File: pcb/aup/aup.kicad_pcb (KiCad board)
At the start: 6 copper layers, 241.9 x 103 mm, 140 parts, among them IC1 MT41K128M16JT-125_K, IC2 88E1512-A0-NNP2C000, J1 DF40C-100DS-0.4V51, J1 DF40C-50DS-0.4V_51, J10 DF40C-50DS-0.4V_51, J11 DF40C-50DS-0.4V_51, J12 DF40C-50DS-0.4V_51, J2 DF40C-100DS-0.4V51, J2 DF40C-50DS-0.4V_51, J3 DF40C-100DS-0.4V51, J3 DF40C-50DS-0.4V_51, J4 DF40C-100DS-0.4V51, J4 DF40C-50DS-0.4V_51, J5 DF40C-40DS-0.4V51, J5 DF40C-50DS-0.4V_51, J6 DF40C-50DS-0.4V_51, J7 DF40C-50DS-0.4V_51, J8 DF40C-50DS-0.4V_51, J9 DF40C-50DS-0.4V_51, Q1 AO3401A, Q2 AO3400A, Q3 AO3401A, U1 XC7A50T-FGG484, U10 TPS2116DRLR, U11 FT2232HQ, U12 93LC56BT-I/OT, U13 MX25L3233FM2, U14 ISL80103IRAJZ-TK, U15 TPS2116DRLR, U2 USBLC6-2SC6, U3 TPS563257DRLR, U5 TPS563257DRLR, U6 ISL80103IRAJZ-TK, U7 TPS563257DRLR, U8 TPS563257DRLR, U9 TPS563257DRLR, Y1 12MHz/20pf

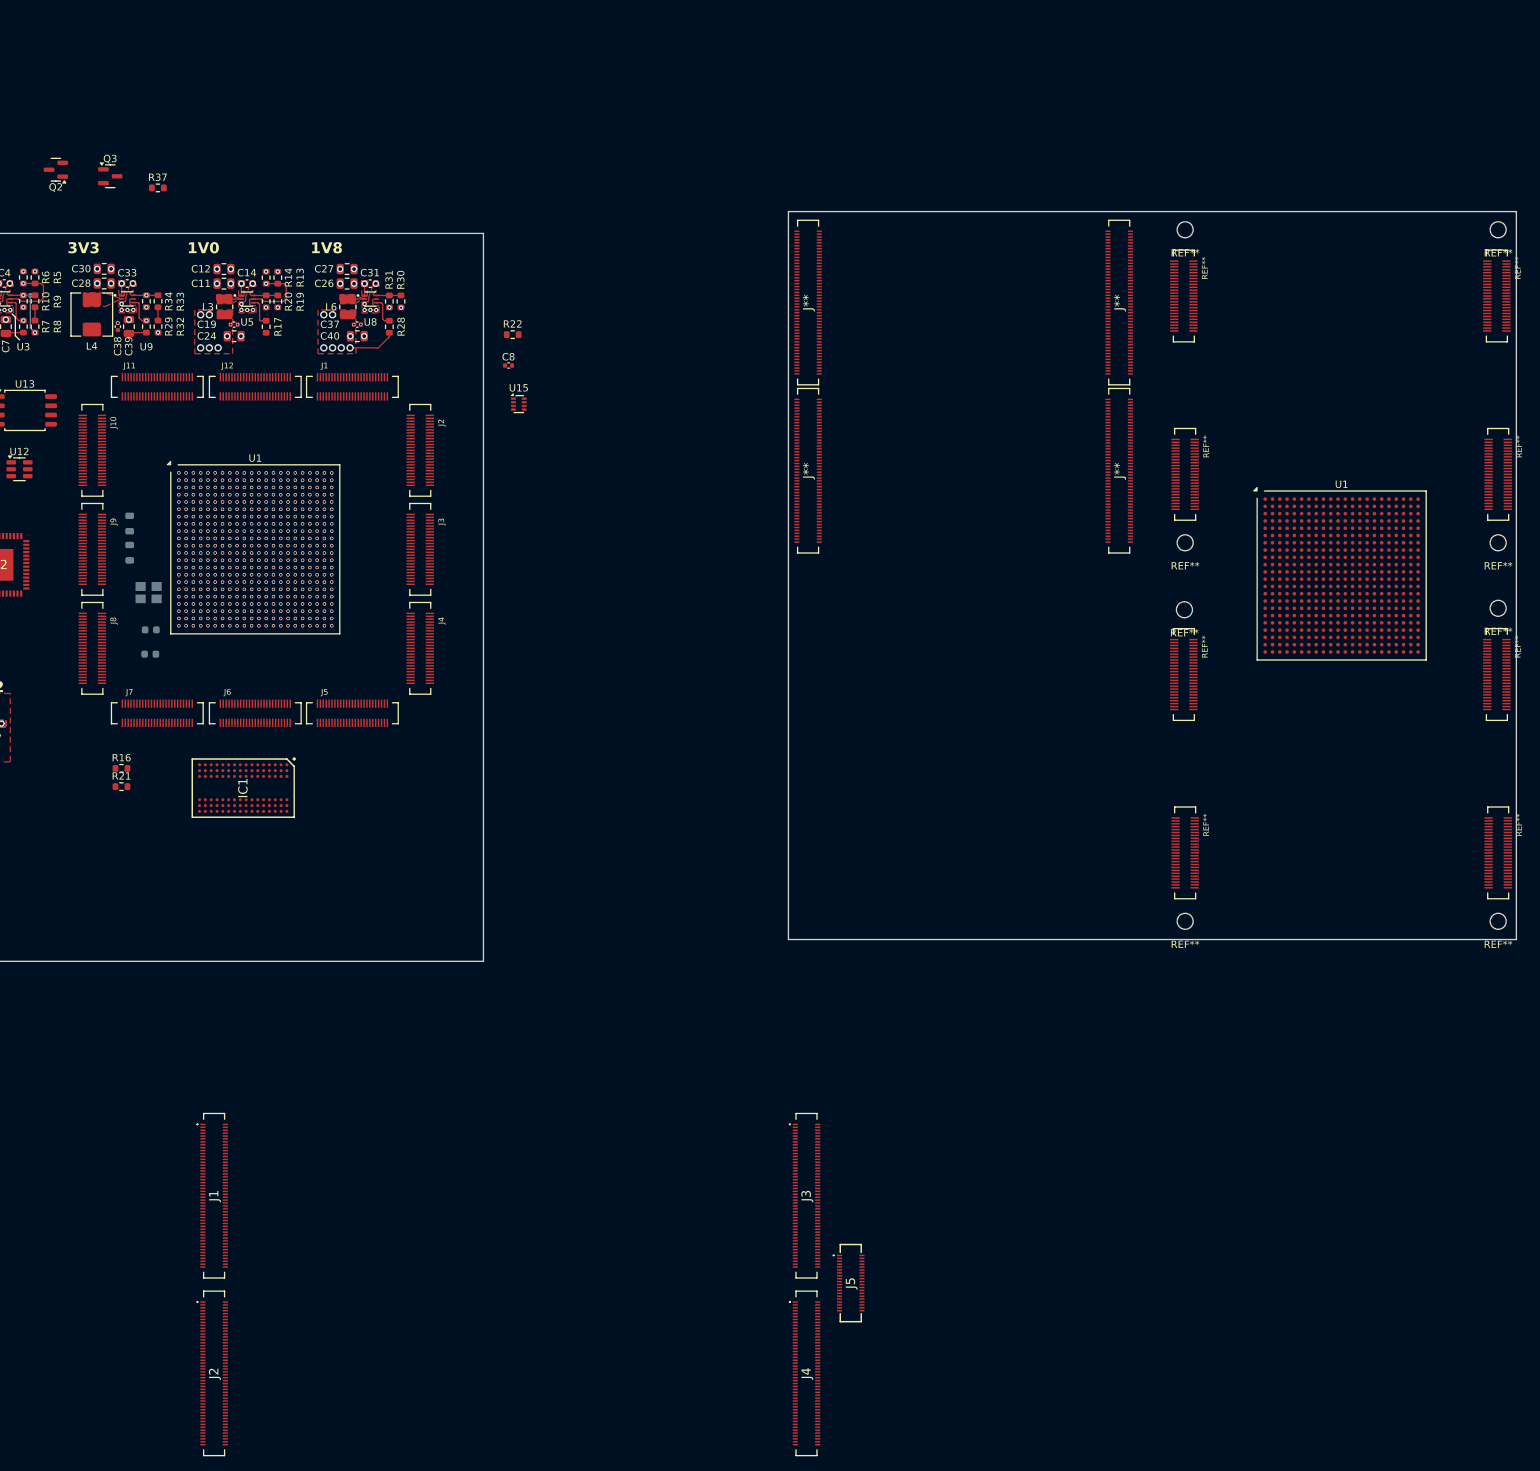
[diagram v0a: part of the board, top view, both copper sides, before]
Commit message: Switch to QSH-60
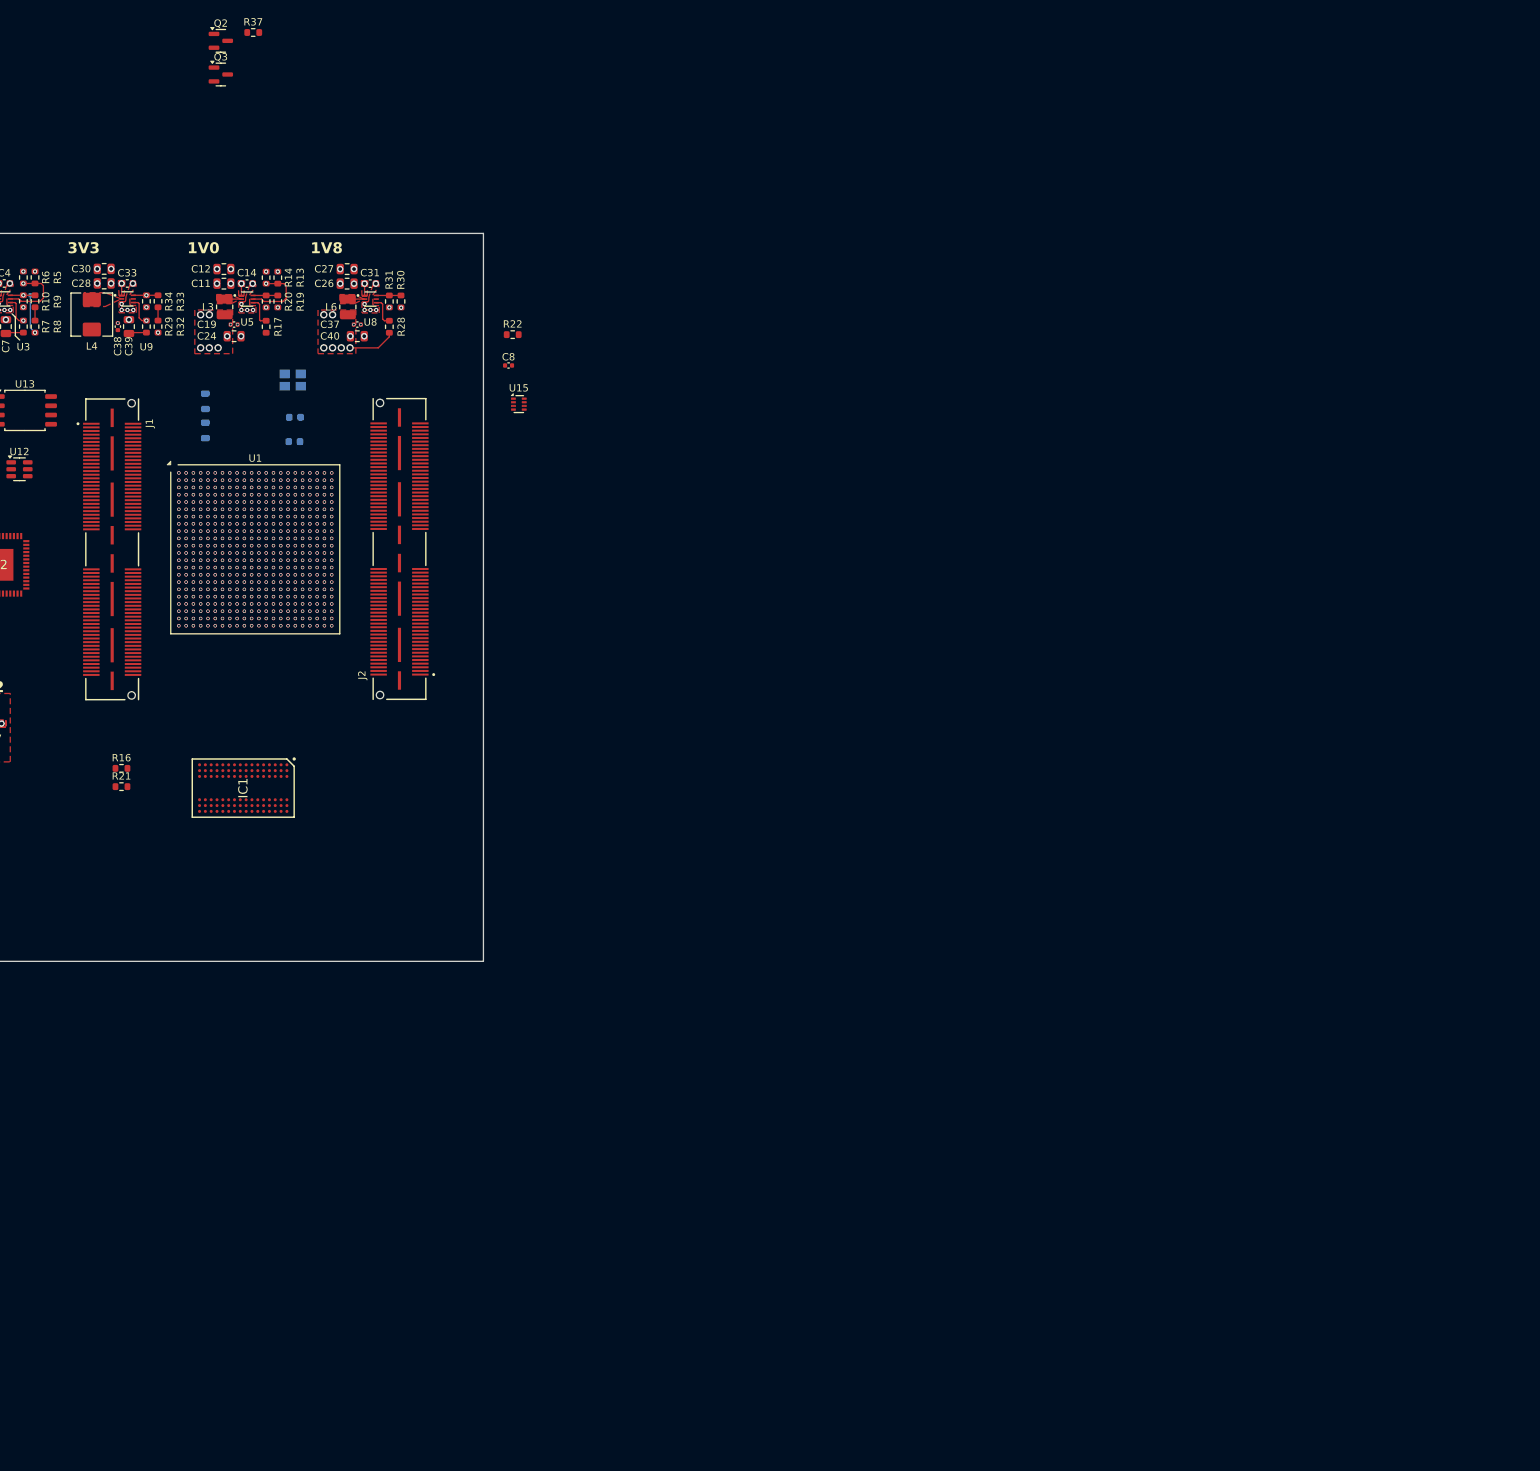
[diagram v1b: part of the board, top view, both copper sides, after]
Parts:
- removed J** (x4): DF40C100DS04V51, !DF40C:DF40C100DS04V51
- removed the J1 at (87.8, 155.8)
- removed the J1 at (106.8, 44.7)
- removed J10, J11, J12, J3, J4, J5, J6, J7, J8, J9: DF40C-50DS-0.4V_51, !DF40C:DF40C50DS04VD1
- removed the J2 at (116.1, 53.4)
- removed the J2 at (87.8, 180.2)
- removed J3, J4: DF40C-100DS-0.4V51, DF40C-100DS-0.4V_51:DF40C100DS04V51
- removed J5: DF40C-40DS-0.4V51, DF40C-40DS-0.4V_51:DF40C40DS04V51
- removed REF** (x8): MountingHole_2.2mm_M2, MountingHole:MountingHole_2.2mm_M2
- removed REF** (x8): DF40C50DS04VD1, !DF40C:DF40C50DS04VD1
- removed the U1 at (242.7, 70.6)
- added J1: QSH-060-01-L-D-A, !Misc:SAMTEC_QSH-060-01-X-D-A, F.Cu at (73.8, 67.0)
- added J2: QSH-060-01-L-D-A, !Misc:SAMTEC_QSH-060-01-X-D-A, F.Cu at (113.3, 67.0)
- moved C44 35.3 mm to (98.9, 48.9)
- moved C43 35.3 mm to (98.8, 52.2)
- moved Y1 35.3 mm to (98.6, 43.8)
- moved Q2 28.8 mm to (88.7, -2.85), turned to 0 degrees
- moved R37 25.0 mm to (93.2, -4.00)
- moved Q3 20.6 mm to (88.7, 1.77)
- moved FB2 19.8 mm to (86.6, 50.7)
- moved FB1 19.8 mm to (86.6, 46.7)
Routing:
- net unconnected-(J2-Pad119): vias 0 -> 2
- net Net-(U1A-IO_0_14): vias 50 -> 51
- net (no net): vias 35 -> 32
- removed copper zone on In2.Cu, net +5V
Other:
- board size 241.9 x 103 mm -> 100 x 100 mm

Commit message: Misc updates - too hard to see in a diff after a delay
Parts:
- added U4: ADP5054, Package_DFN_QFN:QFN-48-1EP_7x7mm_P0.5mm_EP5.15x5.15mm, F.Cu at (163.5, 41.4)
- moved IC1 15.7 mm to (86.9, 84.9)

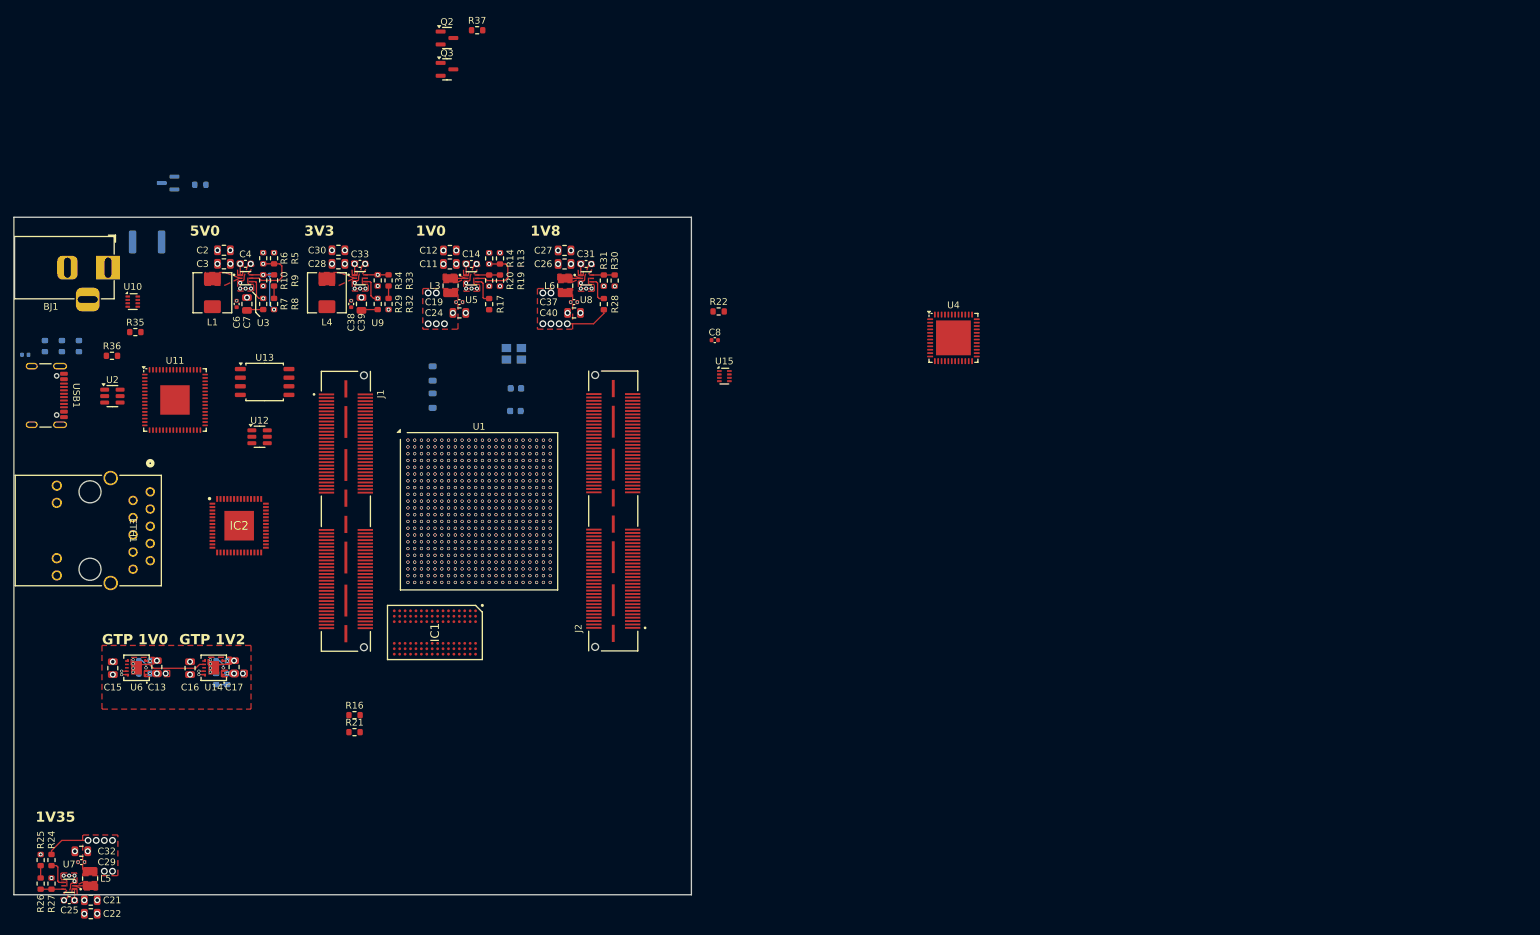
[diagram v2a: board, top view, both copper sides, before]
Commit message: Planning upsized layout
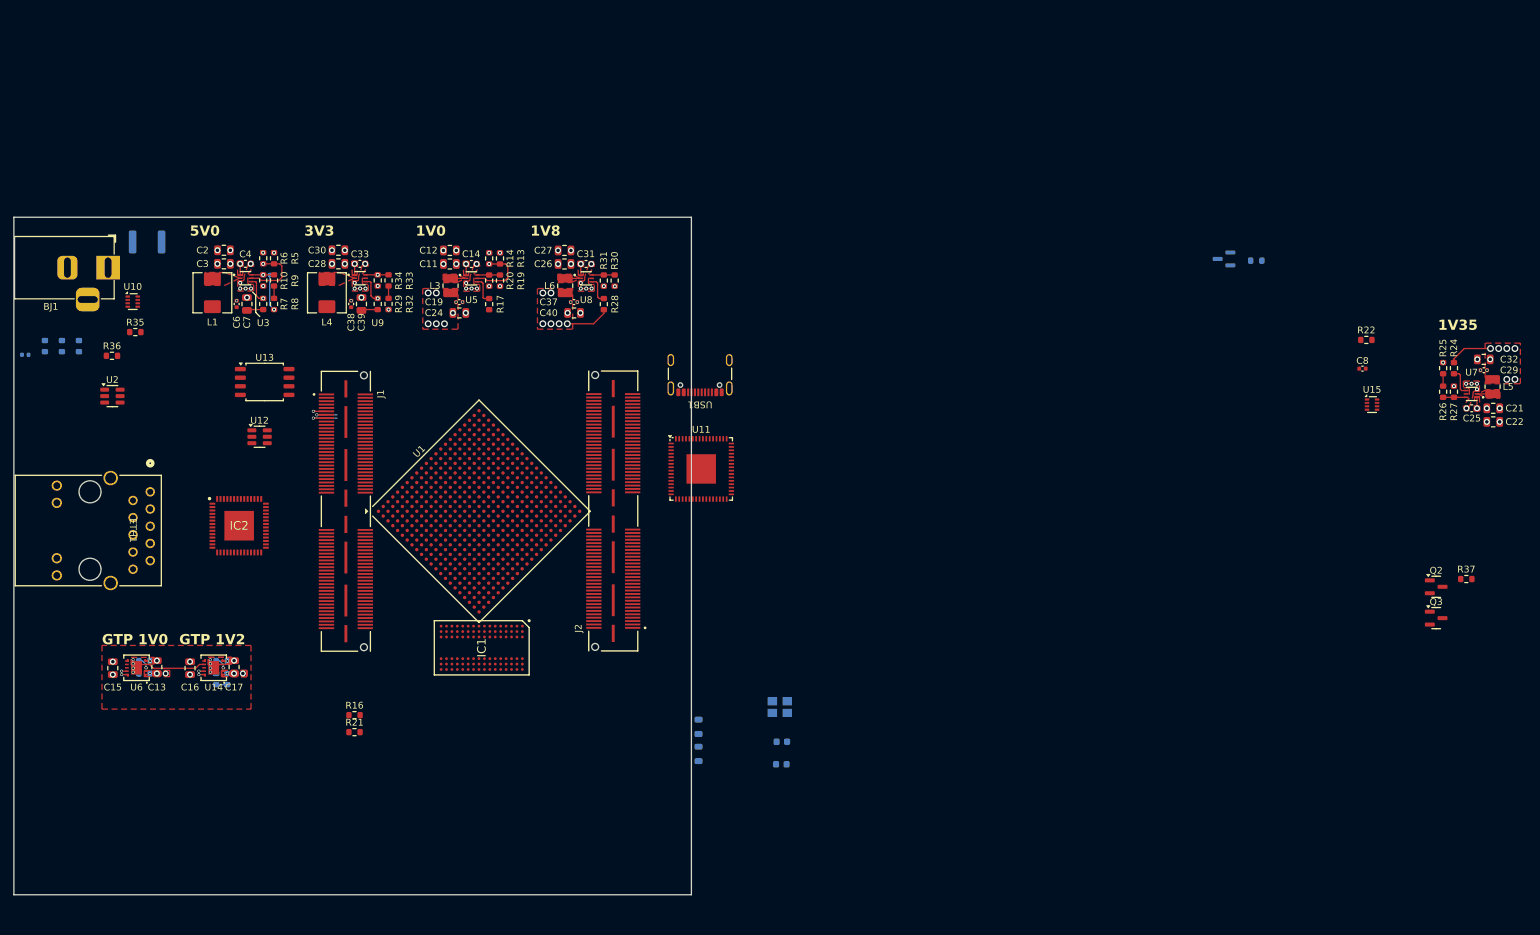
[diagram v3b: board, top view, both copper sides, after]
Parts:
- removed U4: ADP5054, Package_DFN_QFN:QFN-48-1EP_7x7mm_P0.5mm_EP5.15x5.15mm
- moved C21 219.4 mm to (243.2, 51.8)
- moved C22 219.4 mm to (243.2, 53.8)
- moved C25 219.4 mm to (240.0, 51.8)
- moved C29 219.4 mm to (241.8, 46.2)
- moved C32 219.4 mm to (241.8, 44.6)
- moved L5 219.4 mm to (243.1, 48.6)
- moved R24 219.4 mm to (237.3, 45.9)
- moved R25 219.4 mm to (235.8, 45.9)
- moved R26 219.4 mm to (235.8, 49.4)
- moved R27 219.4 mm to (237.4, 49.4)
- moved U7 219.4 mm to (240.0, 49.7)
- moved Q2 167.0 mm to (234.7, 78.1)
- moved Q3 167.0 mm to (234.7, 82.8)
- moved R37 167.0 mm to (239.2, 77.0)
- moved R4 156.3 mm to (208.2, 30.0)
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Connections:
- USB1 pad A1: GND -> (no net)
- USB1 pad A12: GND -> (no net)
- USB1 pad A4: /ext_power/USB_5V -> (no net)
- USB1 pad A5: Net-(USB1-CC1) -> (no net)
- USB1 pad A6: /ext_power/USB_DP -> (no net)
- USB1 pad A7: /ext_power/USB_DN -> (no net)
- USB1 pad A8: unconnected-(USB1-SBU1-PadA8) -> (no net)
- USB1 pad A9: /ext_power/USB_5V -> (no net)
- USB1 pad B1: GND -> (no net)
- USB1 pad B12: GND -> (no net)
- USB1 pad B4: /ext_power/USB_5V -> (no net)
- USB1 pad B5: Net-(USB1-CC2) -> (no net)
- USB1 pad B6: /ext_power/USB_DP -> (no net)
- USB1 pad B7: /ext_power/USB_DN -> (no net)
- USB1 pad B8: unconnected-(USB1-SBU2-PadB8) -> (no net)
- USB1 pad B9: /ext_power/USB_5V -> (no net)
- USB1 pad S1: Net-(USB1-SHIELD) -> (no net)
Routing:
- net +1V0: track 7.93 -> 0.00 mm, vias 25 -> 8
- net /power_reg/PG_3V3: track 11.9 -> 4.02 mm
- net GND: track 24.3 -> 16.4 mm, vias 154 -> 66
- net unconnected-(J1-Pad15): track 0.00 -> 5.44 mm, vias 0 -> 1
- net unconnected-(J1-Pad13): track 0.00 -> 4.41 mm, vias 0 -> 1
- net unconnected-(J1-Pad11): track 0.00 -> 1.94 mm, vias 0 -> 1
- net unconnected-(U1G-VCCBATT_0-PadE12): vias 1 -> 0
- net unconnected-(U1F-VP_0-PadL10): vias 1 -> 0
- net unconnected-(U1F-VN_0-PadM9): vias 1 -> 0
- net unconnected-(U1F-VCCO_0-PadT12): vias 1 -> 0
- net unconnected-(U1F-VCCO_0-PadF12): vias 1 -> 0
- net unconnected-(U1F-TMS_0-PadT13): vias 1 -> 0
- net unconnected-(U1F-TDO_0-PadU13): vias 1 -> 0
- net unconnected-(U1F-TDI_0-PadR13): vias 1 -> 0
- net unconnected-(U1F-TCK_0-PadV12): vias 1 -> 0
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- removed copper zone on In4.Cu, net GND
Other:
- copper layers 6 -> 4

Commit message: More upsized planning
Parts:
- removed BJ1: Barral_Jack_12V, Connector_BarrelJack:BarrelJack_Horizontal
- removed C2, C3: 10uf/50V, Capacitor_SMD:C_0805_2012Metric
- removed C4: 0.1uf/50v, Capacitor_SMD:C_0603_1608Metric
- removed C5: 33pf, Capacitor_SMD:C_0402_1005Metric
- removed C6, C8: 0.1uf, Capacitor_SMD:C_0402_1005Metric
- removed C7: 22uf/25V, Capacitor_SMD:C_0805_2012Metric
- removed ETH1: HR911130A, !Misc:HR911130A_HAN
- removed F1: 2A, Fuse:Fuse_1812_4532Metric
- removed IC2: 88E1512-A0-NNP2C000, !Misc:88E1512-A0-NNP2C000
- removed L1: 2.2uH/5A, Inductor_SMD:L_Sunlord_MWSA0518S
- removed Q1: AO3401A, Package_TO_SOT_SMD:SOT-23
- removed R10, R6: 20K, Resistor_SMD:R_0603_1608Metric
- removed R4, R7, R9: 10K, Resistor_SMD:R_0603_1608Metric
- removed R5: 100K, Resistor_SMD:R_0603_1608Metric
- removed R8: 150K, Resistor_SMD:R_0603_1608Metric
- removed U3: TPS563257DRLR, !Misc:SOT6_DRL_TEX
- U12: moved to B.Cu
- moved C32 123.9 mm to (126.1, 89.0), turned to 0 degrees
- moved L5 123.7 mm to (124.8, 84.9), turned to -90 degrees
- moved C29 122.8 mm to (126.1, 87.4), turned to 0 degrees
- moved C21 122.2 mm to (124.7, 81.8), turned to 180 degrees
- moved C22 121.3 mm to (124.7, 79.8), turned to 180 degrees
- moved U7 117.2 mm to (127.9, 83.9), turned to 0 degrees
- moved C25 116.0 mm to (127.9, 81.8), turned to 0 degrees
- moved R24 114.7 mm to (130.5, 87.7), turned to -90 degrees
- moved R27 112.4 mm to (130.5, 84.2), turned to -90 degrees
- moved R25 111.8 mm to (132.1, 87.7), turned to 90 degrees
- moved R26 109.4 mm to (132.1, 84.2), turned to 90 degrees
- moved U2 99.3 mm to (138.6, 50.8)
- moved U12 70.4 mm to (131.4, 59.2), turned to 180 degrees
- moved U13 67.4 mm to (125.9, 68.9)
- moved C26 60.9 mm to (58.1, 68.0)
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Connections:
- net /ext_power/REG_5V renamed /ext_power/Ext5V
- USB1 pad A1: (no net) -> GND
- USB1 pad A12: (no net) -> GND
- USB1 pad A4: (no net) -> /ext_power/USB_5V
- USB1 pad A5: (no net) -> Net-(USB1-CC1)
- USB1 pad A6: (no net) -> /ext_power/USB_DP
- USB1 pad A7: (no net) -> /ext_power/USB_DN
- USB1 pad A8: (no net) -> unconnected-(USB1-SBU1-PadA8)
- USB1 pad A9: (no net) -> /ext_power/USB_5V
- USB1 pad B1: (no net) -> GND
- USB1 pad B12: (no net) -> GND
- USB1 pad B4: (no net) -> /ext_power/USB_5V
- USB1 pad B5: (no net) -> Net-(USB1-CC2)
- USB1 pad B6: (no net) -> /ext_power/USB_DP
- USB1 pad B7: (no net) -> /ext_power/USB_DN
- USB1 pad B8: (no net) -> unconnected-(USB1-SBU2-PadB8)
- USB1 pad B9: (no net) -> /ext_power/USB_5V
- USB1 pad S1: (no net) -> Net-(USB1-SHIELD)
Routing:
- net /ext_power/EN_5V: track 9.45 -> 0.00 mm, vias 1 -> 0
- net /ext_power/Ext5V: track 7.67 -> 0.00 mm, vias 1 -> 0
- net GND: track 16.4 -> 23.6 mm, vias 66 -> 69
- net /power_reg/PG_Vmgtavcc: track 9.02 -> 2.76 mm
- net unconnected-(J1-Pad15): track 5.44 -> 0.00 mm, vias 1 -> 0
- net unconnected-(J1-Pad13): track 4.41 -> 0.00 mm, vias 1 -> 0
- net Net-(U3-PG): track 4.02 -> 0.00 mm, vias 1 -> 0
- net /ext_power/FB_5V: track 3.37 -> 0.00 mm, vias 1 -> 0
- net unconnected-(J1-Pad11): track 1.94 -> 0.00 mm, vias 1 -> 0
- net Net-(R8-Pad2): track 1.83 -> 0.00 mm
- net /ext_power/PROT_12V: track 1.62 -> 0.00 mm, vias 4 -> 0
- net +Vmgtavcc: track 0.00 -> 1.41 mm, vias 4 -> 5
- net +Vmgtavtt: vias 2 -> 3
- added copper zone on F.Cu, net +Vmgtavcc
- added copper zone on F.Cu, net +Vmgtavtt
- removed copper zone on F.Cu, net /ext_power/PROT_12V
- removed copper zone on F.Cu, net /ext_power/SW_5V
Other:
- board size 100 x 100 mm -> 81 x 50 mm
- copper layers 4 -> 8
- board text removed: "5V0"
